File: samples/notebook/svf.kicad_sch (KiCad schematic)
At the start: 15 parts, among them U1 4069, U2 4069, U3 4069, U4 4069

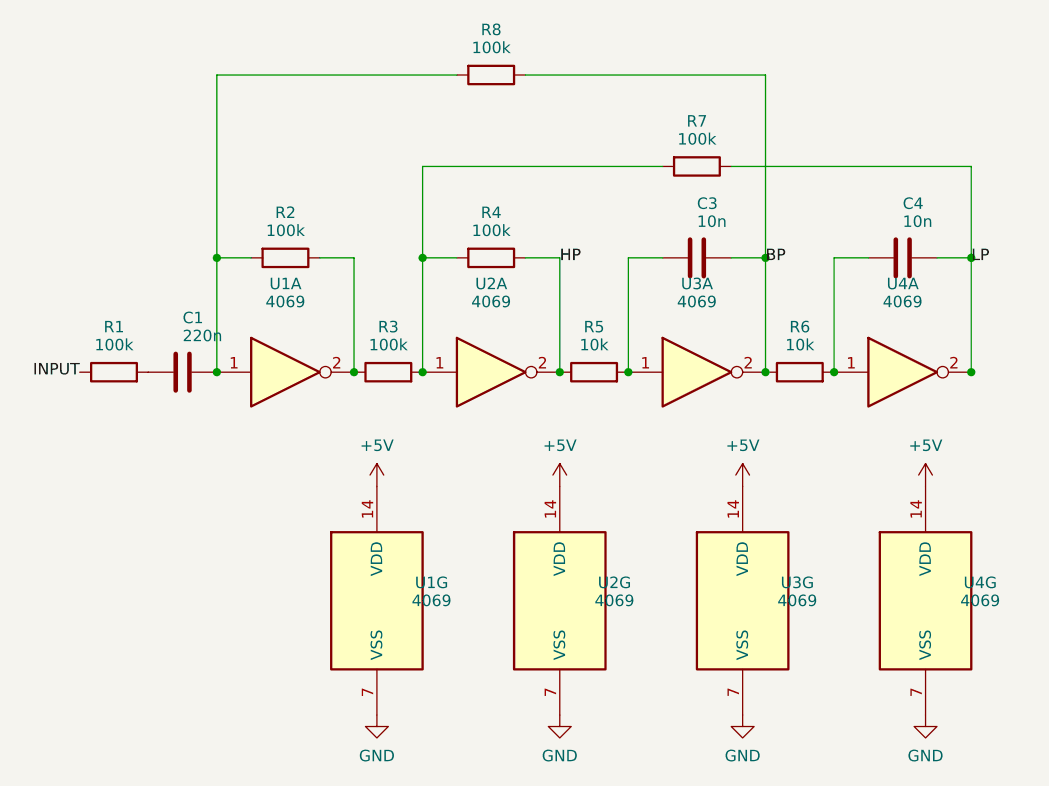
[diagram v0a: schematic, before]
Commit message: update draw arc in plotter and work on docs
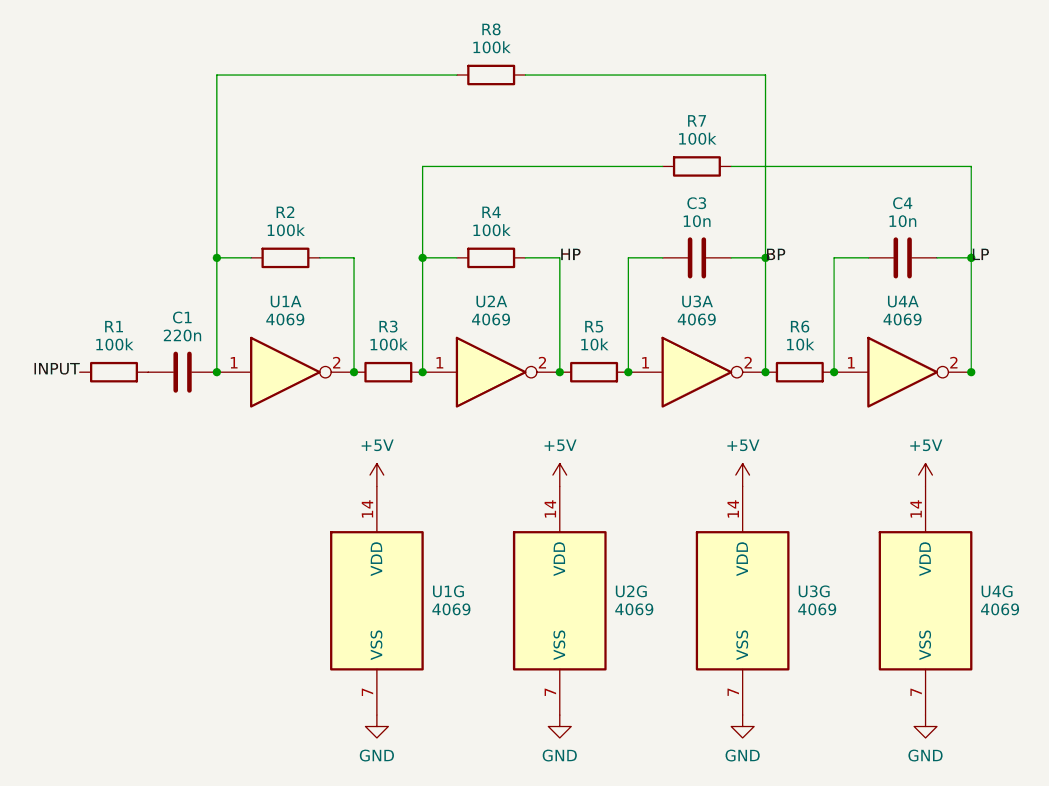
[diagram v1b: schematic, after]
